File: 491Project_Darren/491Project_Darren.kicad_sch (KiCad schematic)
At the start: 48 parts, among them J1 RJ45, J2 RJ45, J3 Conn_01x10_MountingPin

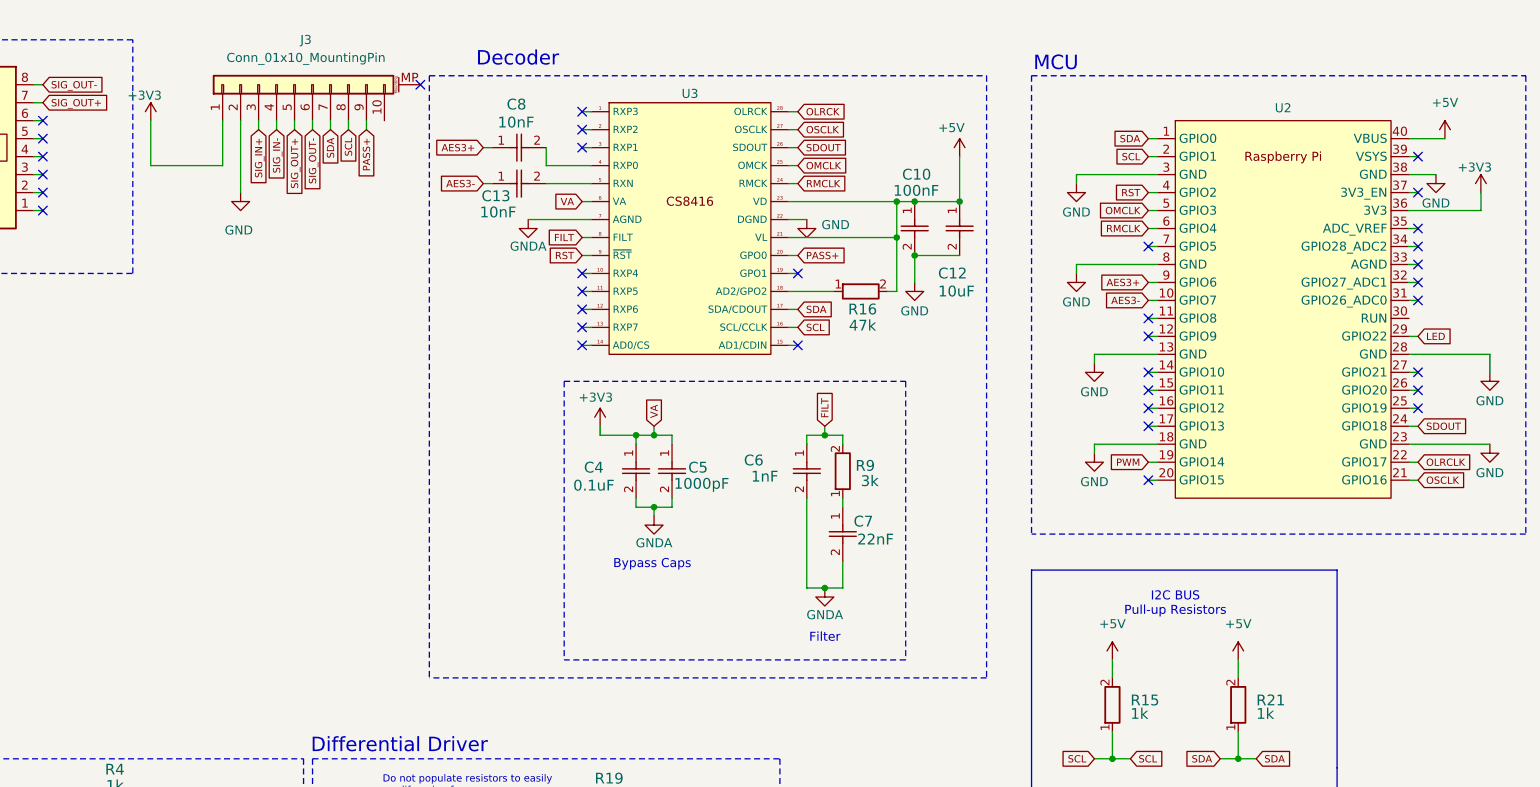
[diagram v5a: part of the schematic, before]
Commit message: fix cutouts
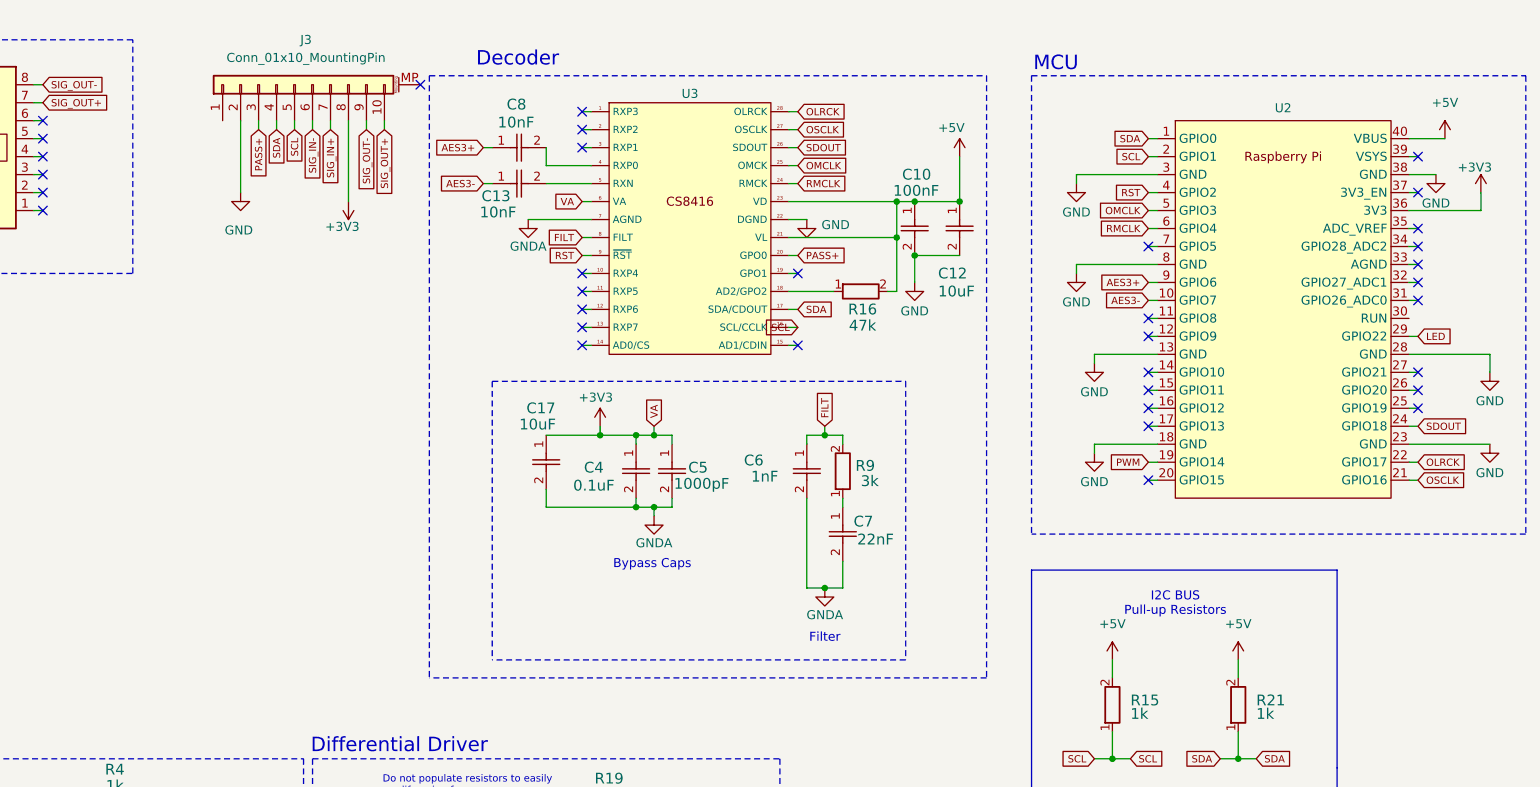
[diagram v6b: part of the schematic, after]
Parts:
- added C17: 10uF, 491_Footprints:CAP_ALUM, symbol 491_Symbols:CAP_ALUM
- J3: footprint Connector_PinHeader_1.27mm:PinHeader_1x11_P1.27mm_Vertical -> Connector_PinHeader_1.27mm:PinHeader_1x10_P1.27mm_Vertical
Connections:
- net OLRCLK is gone; now on net OLRCK: U2.22 (GPIO17)
- net +3V3: now also J3.8 (Pin_8), C17.1; no longer J3.1 (Pin_1)
- net GNDA: now also C17.2
- net PASS+: now also J3.3 (Pin_3); no longer J3.9 (Pin_9)
- net SCL: now also J3.5 (Pin_5); no longer J3.8 (Pin_8)
- net SDA: now also J3.4 (Pin_4); no longer J3.7 (Pin_7)
- net SIG_IN+: now also J3.7 (Pin_7); no longer J3.3 (Pin_3)
- net SIG_IN-: now also J3.6 (Pin_6); no longer J3.4 (Pin_4)
- net SIG_OUT+: now also J3.10 (Pin_10); no longer J3.5 (Pin_5)
- net SIG_OUT-: now also J3.9 (Pin_9); no longer J3.6 (Pin_6)
